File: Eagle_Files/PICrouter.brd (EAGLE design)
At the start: 64.8 x 29.8 mm, 76 parts, among them IC1 PIC32MX675F512H, IC2 48M033F, IC3 DP83848, J1 POWER_JACK, Q1 20MHz, X2 USB_B

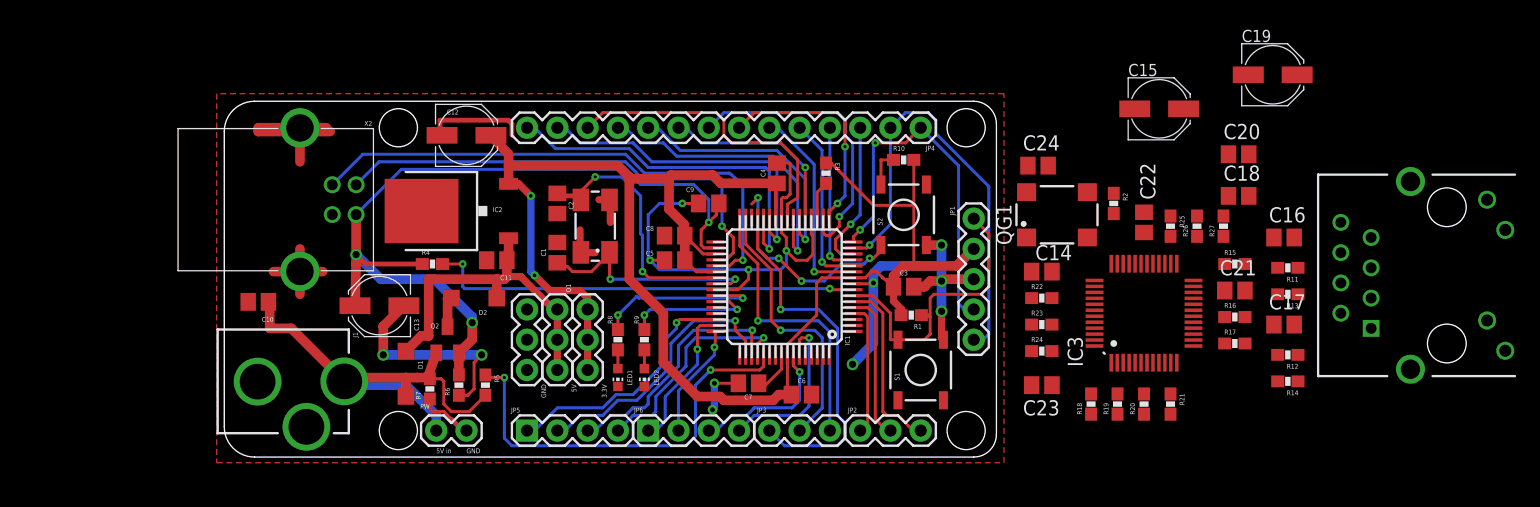
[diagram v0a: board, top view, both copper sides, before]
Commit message: Released PICrouter schematic and board v0.5.
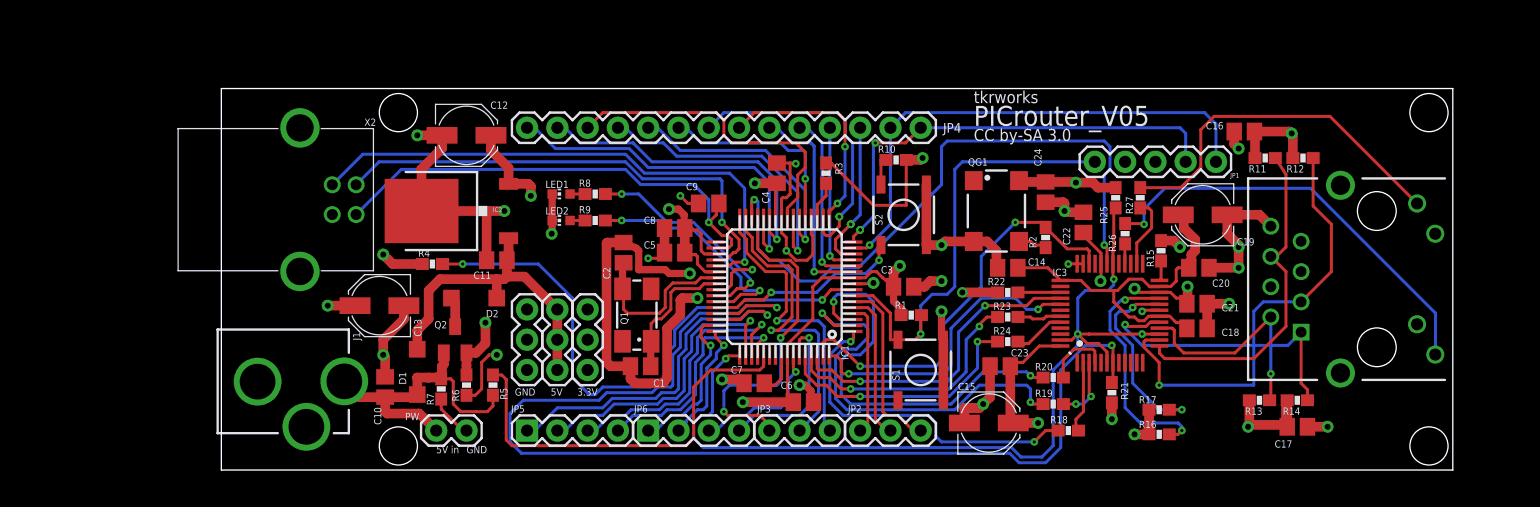
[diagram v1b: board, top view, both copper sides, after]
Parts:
- moved C15 30.0 mm to (68.6, 4.45)
- moved R12 16.6 mm to (94.9, 26.7)
- moved LED1 16.1 mm to (32.7, 23.7), turned to 90 degrees
- moved LED2 14.9 mm to (32.7, 21.4), turned to 90 degrees
- moved C19 13.1 mm to (86.5, 21.9), turned to 180 degrees
- moved C10 12.8 mm to (17.9, 7.46), turned to 90 degrees
- moved R8 12.4 mm to (35.6, 23.7), turned to 0 degrees
- moved C1 11.8 mm to (39.4, 9.21), turned to 180 degrees
- moved R16 11.7 mm to (82.9, 3.49), turned to 180 degrees
- moved C18 11.6 mm to (86.0, 12.4)
- moved JP1 11.2 mm to (77.5, 26.4), turned to 0 degrees
- moved R9 10.8 mm to (35.6, 21.4), turned to 0 degrees
- moved C20 10.1 mm to (86.2, 17.5)
- moved C16 9.49 mm to (90.0, 28.9), turned to 180 degrees
- moved R11 9.40 mm to (91.8, 26.7)
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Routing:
- net GND: track 139.4 -> 387.6 mm, vias 13 -> 30
- net VDD: track 140.9 -> 366.4 mm, vias 2 -> 16
- net EINT: track 0.00 -> 98.6 mm, vias 0 -> 2
- net EMDIO: track 0.00 -> 64.2 mm, vias 0 -> 2
- net EMDC: track 0.00 -> 53.6 mm, vias 0 -> 2
- net RDP: track 0.00 -> 37.7 mm, vias 0 -> 1
- net N$55: track 0.00 -> 35.9 mm, vias 0 -> 1
- net ETXD1: track 0.00 -> 35.0 mm, vias 0 -> 2
- net ETXD0: track 0.00 -> 35.0 mm, vias 0 -> 2
- net EREFCLK: track 0.00 -> 34.6 mm, vias 0 -> 2
- net PFBOUT: track 0.00 -> 30.7 mm
- net N$62: track 0.00 -> 30.6 mm
- net ETXEN: track 0.00 -> 28.7 mm, vias 0 -> 2
- net RDM: track 0.00 -> 28.3 mm
- net ECRSDV: track 0.00 -> 26.7 mm, vias 0 -> 2
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- added copper zone on layer 2, net GND
- added copper zone on layer 3, net VDD
- removed copper zone on layer 1, net GND
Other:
- board size 64.8 x 29.8 mm -> 103.3 x 32 mm
- board text added: "CC by-SA 3.0"
- board text added: "PICrouter_V05"
- board text removed: "PICrouter"
- board text removed: "v0.3 / CC BY-SA"

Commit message: Released PICrouter schematic and board v0.6.
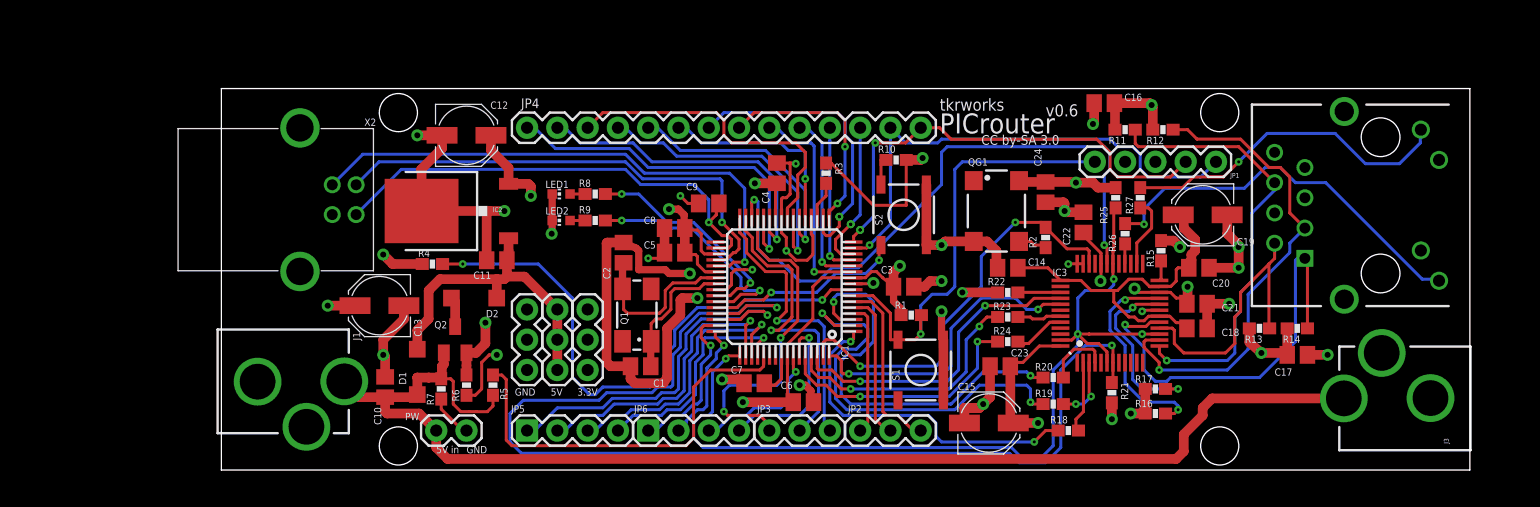
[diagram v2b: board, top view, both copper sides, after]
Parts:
- added J3: POWER_JACK, SparkFun:POWER_JACK_PTH_LOCK
- moved C16 12.0 mm to (78.3, 31.3)
- moved R12 12.0 mm to (83.2, 29.1)
- moved R11 12.0 mm to (80.0, 29.1)
- moved J2 6.20 mm to (101.4, 22.7)
- moved R13 6.03 mm to (91.3, 12.4)
- moved R14 6.03 mm to (94.5, 12.4)
- moved C17 6.03 mm to (94.5, 10.2)
- moved R17 1.77 mm to (82.5, 7.30)
- moved R16 1.77 mm to (82.5, 5.24)
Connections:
- net GND: now also J3.GND
- net N$46: now also J3.PWR
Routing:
- net VDD: track 366.4 -> 120.5 mm
- net GND: track 387.6 -> 171.3 mm
- net N$46: track 26.4 -> 107.7 mm
- net TDP: track 25.2 -> 35.7 mm
- net RDM: track 28.3 -> 37.3 mm, vias 0 -> 1
- net TDM: track 19.3 -> 23.7 mm, vias 1 -> 0
- net RDP: track 37.7 -> 40.8 mm
- net N$55: track 35.9 -> 33.0 mm
- net N$62: track 30.6 -> 28.3 mm, vias 0 -> 1
- net N$47: track 20.1 -> 17.9 mm
- net N$48: track 16.5 -> 15.2 mm
- net EMDC: track 53.6 -> 52.7 mm
- net N$3: track 43.4 -> 42.6 mm
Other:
- board size 103.3 x 32 mm -> 104.7 x 32 mm
- board text added: "PICrouter"
- board text added: "v0.6"
- board text removed: "PICrouter_V05"

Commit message: Released PICrouter schematic and board v0.7.
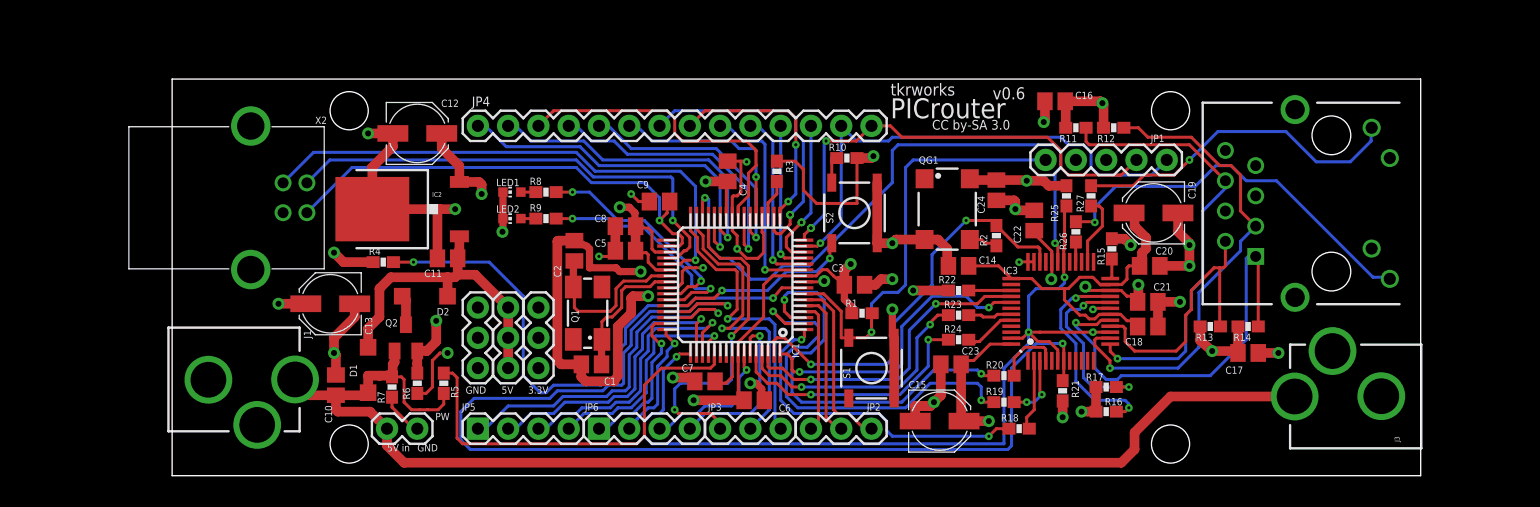
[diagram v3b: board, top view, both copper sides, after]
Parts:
- C14, C16, C17, C18, C20, C21, C22, C23, C24: value (none) -> 0.1uF
- moved R11 4.13 mm to (75.9, 29.2)
- moved R19 4.13 mm to (69.8, 6.19)
- moved R20 4.13 mm to (69.8, 8.41)
- moved R21 4.13 mm to (74.8, 7.14)
- moved R26 4.13 mm to (75.9, 20.5)
- moved C3 4.13 mm to (57.3, 16.0)
- moved C6 4.13 mm to (48.9, 6.35)
- moved C7 4.13 mm to (44.8, 7.94)
- moved IC1 4.13 mm to (47.3, 16.0)
- moved JP4 4.13 mm to (58.7, 29.4)
- moved JP6 4.13 mm to (35.9, 3.97)
- moved Q1 4.13 mm to (34.9, 13.7)
- moved R10 4.13 mm to (56.7, 26.7)
- moved R3 4.13 mm to (50.8, 25.6)
- moved S1 4.13 mm to (58.7, 9.05)
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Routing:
- net VDD: track 120.5 -> 121.6 mm
- net EMDIO: track 64.2 -> 63.4 mm
- net EINT: track 98.6 -> 97.8 mm
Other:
- board size 104.7 x 32 mm -> 104.7 x 33.3 mm

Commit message: Released PICrouter schematic and board v0.71.
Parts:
- removed J1: POWER_JACK, SparkFun:POWER_JACK_PTH_LOCK
- removed X2: USB_B, con-cypressindustries:85-32004-10X
- added C25: 100uF, rcl:PANASONIC_C
- added C26: 0.1uF, rcl:C2012
- added F1: PTCSMD, SparkFun:PTC-1206
- added U1: USB+SHIELD, SparkFun:USB-B-PTH
- added X1: USB-A-H, SparkFun:USB-A-H
- IC1: device PIC:TQFP64-10X10 -> PIC.rpt:TQFP64-10X10
- moved C12 11.1 mm to (31.1, 25.1), turned to 180 degrees
- moved LED1 6.19 mm to (28.6, 17.6), turned to 180 degrees
- moved LED2 4.47 mm to (30.6, 17.6), turned to 180 degrees
- moved JP1 4.46 mm to (68.9, 26.8)
- moved R8 4.39 mm to (28.6, 20.5), turned to 90 degrees
- moved PW 2.54 mm to (20.6, 3.97), turned to 90 degrees
- moved R7 2.35 mm to (18.5, 9.81)
- moved C10 2.16 mm to (14.4, 9.68)
- moved R5 2.03 mm to (22.9, 9.81)
- moved R6 2.03 mm to (20.6, 9.81)
- moved Q2 1.75 mm to (19.5, 13.3)
- moved C13 1.75 mm to (13.3, 16.2)
- moved D1 1.75 mm to (16.5, 10.6)
- moved IC2 1.44 mm to (19.2, 23.8)
- moved R9 1.37 mm to (30.6, 20.5), turned to 90 degrees
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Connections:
- removed net N$61: C13.+, C9.2, IC1.34, Q2.2, R4.1, R6.2, X2.1
- new net N$50: C13.+, C25.+, C9.2, F1.1, IC1.34, Q2.2, R4.1, R6.2, U1.VBUS, X1.VBUS
- net GND: now also C25.-, C26.2, U1.GND, U1.S1, U1.S2, X1.GND, X1.GND2, X1.GND3; no longer J1.GND, X2.4
- net N$45: now also U1.D-, X1.D-; no longer X2.2
- net N$46: no longer J1.PWR
- net N$5: now also U1.D+, X1.D+; no longer X2.3
- net VCC: now also F1.2
- net VDD: now also C26.1
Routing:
- net N$50: track 0.00 -> 117.7 mm, vias 0 -> 4
- net N$61: track 76.6 -> 0.00 mm, vias 4 -> 0
- net N$45: track 40.8 -> 67.4 mm
- net N$5: track 45.6 -> 69.5 mm
- net VCC: track 27.6 -> 41.4 mm, vias 0 -> 2
- net VDD: track 121.6 -> 130.9 mm, vias 16 -> 18
- net N$3: track 42.6 -> 36.8 mm
- net N$4: track 38.7 -> 34.0 mm
- net N$6: track 38.0 -> 33.7 mm
- net N$51: track 0.00 -> 4.13 mm
- net N$13: track 18.8 -> 22.9 mm
- net N$44: track 0.00 -> 3.35 mm
- net N$46: track 107.7 -> 105.6 mm
- net N$11: track 34.3 -> 36.3 mm
- net N$14: track 20.0 -> 21.8 mm
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- added copper zone on layer 16, net GND
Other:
- board size 104.7 x 33.3 mm -> 105.5 x 34 mm
- board text added: "v0.8"
- board text removed: "v0.6"

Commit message: Released PICrouter schematic and board v0.8.
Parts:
- removed JP1: (no value), SparkFun:1X05
- removed JP2: SPI2, SparkFun:1X03
- removed JP3: SPI4, SparkFun:1X03
- removed JP4: AN, SparkFun:1X14
- removed JP5: OC, SparkFun:1X04
- removed JP6: I/O, SparkFun:1X04
- added AN: (no value), SparkFun:1X14
- added I/O, OC: (no value), SparkFun:1X04
- added ICSP: (no value), SparkFun:1X05
- added SPI2, SPI4: (no value), SparkFun:1X03
- C13: value 100uF -> 10uF
- C25: value 100uF -> 150uF
- U1: value USB+SHIELD -> DEVICE
- moved PW 3.18 mm to (19.3, 6.85), turned to 270 degrees
- moved C10 2.92 mm to (15.1, 6.85), turned to 180 degrees
- moved R12 2.54 mm to (77.3, 31.2), turned to 90 degrees
- moved J2 2.39 mm to (95.0, 23.2)
- moved C17 2.39 mm to (88.0, 10.7)
- moved J3 2.39 mm to (105.7, 7.01)
- moved R13 2.39 mm to (84.8, 12.9)
- moved R14 2.39 mm to (88.0, 12.9)
- moved R16 2.19 mm to (76.3, 5.99)
- moved C13 1.59 mm to (12.0, 17.0)
- moved R17 1.47 mm to (77.1, 8.06)
- moved C18 1.39 mm to (80.6, 12.9)
- moved C21 1.39 mm to (80.6, 14.9)
- moved R18 1.39 mm to (69.8, 4.31)
- moved R22 1.39 mm to (64.7, 15.9)
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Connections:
- net GND: now also ICSP.3; no longer JP1.3
- net N$18: now also AN.3; no longer JP4.3
- net N$19: now also AN.4; no longer JP4.4
- net N$20: now also AN.5; no longer JP4.5
- net N$21: now also AN.6; no longer JP4.6
- net N$22: now also AN.7; no longer JP4.7
- net N$23: now also AN.8; no longer JP4.8
- net N$24: now also AN.9; no longer JP4.9
- net N$25: now also AN.10; no longer JP4.10
- net N$26: now also AN.11; no longer JP4.11
- net N$27: now also AN.12; no longer JP4.12
- net N$28: now also AN.13; no longer JP4.13
- net N$29: now also AN.14; no longer JP4.14
- net N$3: now also AN.2, ICSP.5; no longer JP1.5, JP4.2
- net N$30: now also SPI2.1; no longer JP2.1
- net N$31: now also SPI2.2; no longer JP2.2
- net N$32: now also SPI2.3; no longer JP2.3
- net N$33: now also SPI4.2; no longer JP3.2
- net N$34: now also SPI4.3; no longer JP3.3
- net N$35: now also SPI4.1; no longer JP3.1
- net N$36: now also OC.1; no longer JP5.1
- net N$37: now also I/O.1; no longer JP6.1
- net N$38: now also OC.2; no longer JP5.2
- net N$39: now also OC.3; no longer JP5.3
- net N$4: now also AN.1, ICSP.4; no longer JP1.4, JP4.1
- net N$40: now also OC.4; no longer JP5.4
- net N$41: now also I/O.2; no longer JP6.2
- net N$42: now also I/O.3; no longer JP6.3
- net N$43: now also I/O.4; no longer JP6.4
- net N$6: now also ICSP.1; no longer JP1.1
- net VDD: now also ICSP.2; no longer JP1.2
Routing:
- net N$50: track 117.7 -> 106.7 mm, vias 4 -> 3
- net GND: track 169.5 -> 164.6 mm, vias 33 -> 35
- net VCC: track 41.4 -> 36.7 mm
- net N$45: track 67.4 -> 70.6 mm
- net N$55: track 33.0 -> 35.1 mm
- net RDM: track 37.1 -> 35.1 mm
- net N$5: track 69.5 -> 67.5 mm
- net PFBOUT: track 31.0 -> 29.4 mm
- net TDP: track 35.7 -> 34.4 mm
- net N$12: track 49.1 -> 48.1 mm
- net N$47: track 17.9 -> 17.1 mm
- net VDD: track 130.9 -> 130.2 mm
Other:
- board size 105.5 x 34 mm -> 101.8 x 34 mm
- board text added: "/* Bridge between OSC and USB_MIDI */"
- board text added: "HOST"
- board text added: "v0.8/CC by-SA 3.0"
- board text removed: "CC by-SA 3.0"
- board text removed: "v0.8"

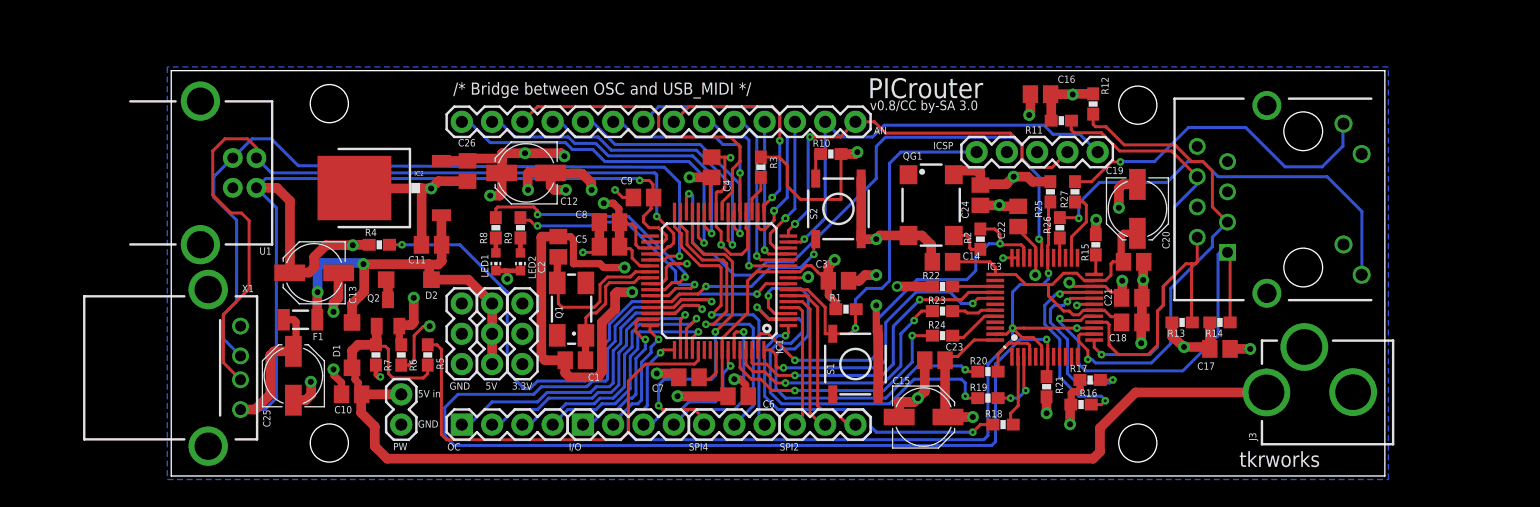
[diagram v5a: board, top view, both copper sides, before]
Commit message: Released PICrouter schematic and board v0.9.
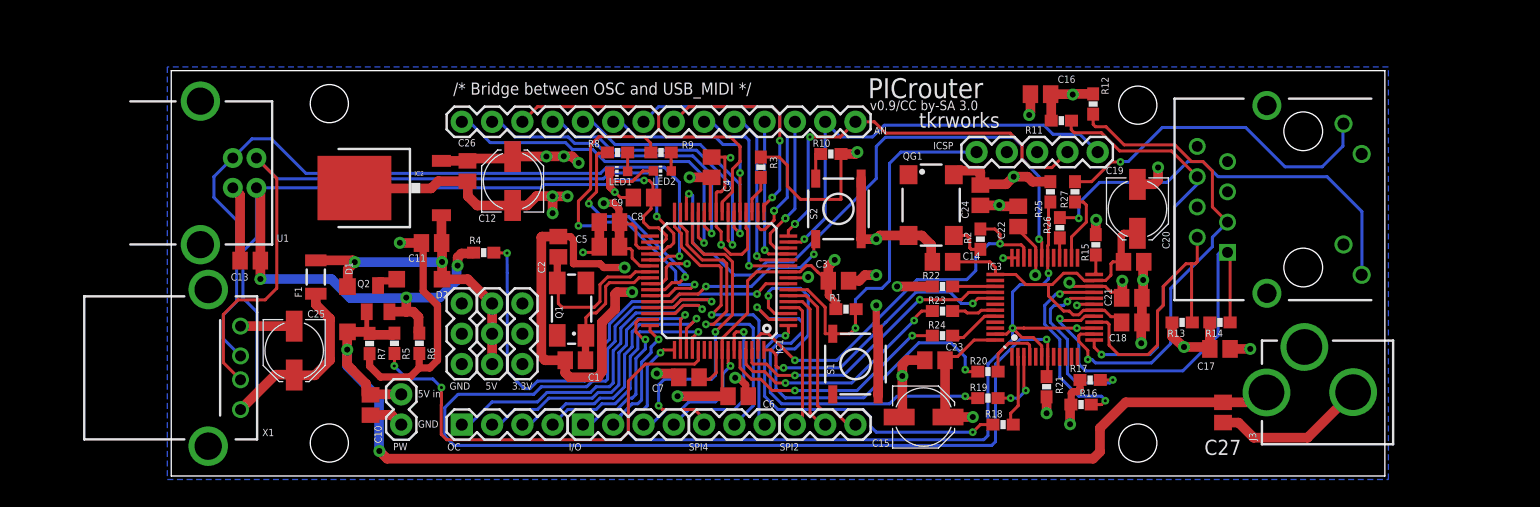
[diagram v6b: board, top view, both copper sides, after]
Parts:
- added C27: 0.1uF, rcl:C2012
- C13: device rcl:PANASONIC_C -> rcl:C2012
- moved LED2 14.1 mm to (41.2, 25.6), turned to 90 degrees
- moved R9 13.4 mm to (41.1, 27.1), turned to 180 degrees
- moved LED1 12.8 mm to (37.5, 25.5), turned to 90 degrees
- moved R8 12.0 mm to (37.4, 27.1), turned to 180 degrees
- moved R4 8.79 mm to (26.2, 18.7)
- moved C13 5.46 mm to (6.62, 18.1)
- moved F1 3.80 mm to (12.1, 16.7), turned to 90 degrees
- moved D1 3.03 mm to (14.8, 14.0)
- moved R5 2.96 mm to (18.7, 11.1), turned to 90 degrees
- moved C25 2.11 mm to (10.3, 10.5), turned to 270 degrees
- moved C10 1.82 mm to (16.7, 5.96), turned to 270 degrees
- moved R6 1.80 mm to (20.8, 11.1)
- moved Q2 1.46 mm to (17.3, 14.9)
- moved C12 1.33 mm to (28.6, 24.7), turned to 90 degrees
- moved R7 1.10 mm to (16.6, 11.1)
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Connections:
- net GND: now also C13.2, C27.2; no longer C13.-
- net N$46: now also C27.1
- net N$50: now also C13.1; no longer C13.+
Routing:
- net GND: track 164.6 -> 204.2 mm, vias 35 -> 29
- net N$14: track 21.8 -> 30.2 mm
- net VCC: track 36.7 -> 28.7 mm
- net N$12: track 48.1 -> 41.0 mm
- net N$50: track 106.7 -> 111.3 mm, vias 3 -> 4
- net N$45: track 70.6 -> 66.3 mm
- net N$51: track 4.13 -> 0.00 mm
- net N$44: track 3.35 -> 0.00 mm
- net N$13: track 22.9 -> 19.5 mm
- net N$46: track 105.6 -> 102.3 mm, vias 0 -> 2
- net VDD: track 130.2 -> 127.1 mm
- net ETXD1: track 35.0 -> 37.2 mm
- net ECRSDV: track 26.7 -> 24.8 mm
- net ERXERR: track 25.6 -> 23.8 mm
- net ETXD0: track 35.0 -> 33.2 mm
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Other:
- board text added: "v0.9/CC by-SA 3.0"
- board text removed: "v0.8/CC by-SA 3.0"
